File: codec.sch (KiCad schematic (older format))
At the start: 48 parts, among them J10 Audio-Jack-3, J11 MicBias, J8 Audio-Jack-3, J9 Audio-Jack-3, U2 CS4245

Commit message: [codec] Sort the input filters and add comp. values
The input filter schematic was wrong, it was using the
output's LP filter circuit (copy/paste error). All components
now have values, as per CS4245's datasheet.
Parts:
- C25, C29, C31, C33, C35, C44, C53, C54: value CP -> 10uF
- C26, C27, C28, C45, C46, C47, C48, C51, C52: value C -> 0.1uF
- C30, C32, C34, C36: value C -> 1.8nF
- C37, C39: value CP -> 3.3uF
- C41, C49, C50: value CP -> 47uF
- C42, C43: value C -> 2.2nF
- R36, R37, R38, R39, R40, R41, R42, R43: value R -> 100
- R44, R47: value R -> 470
- R45, R46: value R -> 10k
- R48: value R -> Rx
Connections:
- wire segments 87 -> 85
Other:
- moved on the sheet: C29, C30, C31, C32, C33, C34, C35, C36, R36, R37, R38, R39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

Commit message: Add power regulators with 5, 3 and 3.3V.
In addition, the connector is now as short as needed.
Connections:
- net labels added: 3.3V, 3V, 5V
- net labels removed: +3.3V, VCC
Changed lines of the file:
@@
 $EndComp
 $Comp
-L GND #PWR029
+L GND #PWR027
 U 1 1 5A0BFF3A
 P 4550 2150
-F 0 "#PWR029" H 4550 1900 50  0001 C CNN
+F 0 "#PWR027" H 4550 1900 50  0001 C CNN
 F 1 "GND" H 4550 2000 50  0000 C CNN
 F 2 "" H 4550 2150 50  0001 C CNN
@@
 $EndComp
 $Comp
-L GND #PWR030
+L GND #PWR028
 U 1 1 5A0C011B
 P 4250 5700
-F 0 "#PWR030" H 4250 5450 50  0001 C CNN
+F 0 "#PWR028" H 4250 5450 50  0001 C CNN
 F 1 "GND" H 4250 5550 50  0000 C CNN
 F 2 "" H 4250 5700 50  0001 C CNN
 F 3 "" H 4250 5700 50  0001 C CNN
 	1    4250 5700
-	1    0    0    -1
-$EndComp
-$Comp
-L +3.3V #PWR031
-U 1 1 5A0C0141
-P 4250 5400
-F 0 "#PWR031" H 4250 5250 50  0001 C CNN
-F 1 "+3.3V" H 4250 5540 50  0000 C CNN
-F 2 "" H 4250 5400 50  0001 C CNN
-F 3 "" H 4250 5400 50  0001 C CNN
-	1    4250 5400
 	1    0    0    -1
 $EndComp
@@
 $EndComp
 $Comp
-L GND #PWR032
+L GND #PWR029
 U 1 1 5A0C08B4
 P 5850 7150
-F 0 "#PWR032" H 5850 6900 50  0001 C CNN
+F 0 "#PWR029" H 5850 6900 50  0001 C CNN
 F 1 "GND" H 5850 7000 50  0000 C CNN
 F 2 "" H 5850 7150 50  0001 C CNN
@@
 AGND2
 $Comp
-L GND #PWR033
+L GND #PWR030
 U 1 1 5A0C1788
 P 7350 5250
-F 0 "#PWR033" H 7350 5000 50  0001 C CNN
+F 0 "#PWR030" H 7350 5000 50  0001 C CNN
 F 1 "GND" H 7350 5100 50  0000 C CNN
 F 2 "" H 7350 5250 50  0001 C CNN
@@
 $EndComp
 $Comp
-L GND #PWR034
+L GND #PWR031
 U 1 1 5A0C2BFF
 P 8000 4300
-F 0 "#PWR034" H 8000 4050 50  0001 C CNN
+F 0 "#PWR031" H 8000 4050 50  0001 C CNN
 F 1 "GND" H 8000 4150 50  0001 C CNN
 F 2 "" H 8000 4300 50  0001 C CNN
@@
 $EndComp
 $Comp
-L GND #PWR035
+L GND #PWR032
 U 1 1 5A0C2DDC
 P 9000 4050
-F 0 "#PWR035" H 9000 3800 50  0001 C CNN
+F 0 "#PWR032" H 9000 3800 50  0001 C CNN
 F 1 "GND" H 9000 3900 50  0000 C CNN
 F 2 "" H 9000 4050 50  0001 C CNN
@@
 $EndComp
 $Comp
-L GND #PWR036
+L GND #PWR033
 U 1 1 5A0C36C8
 P 7250 2600
-F 0 "#PWR036" H 7250 2350 50  0001 C CNN
+F 0 "#PWR033" H 7250 2350 50  0001 C CNN
 F 1 "GND" H 7250 2450 50  0001 C CNN
 F 2 "" H 7250 2600 50  0001 C CNN
@@
 $EndComp
 $Comp
-L GND #PWR037
+L GND #PWR034
 U 1 1 5A0C3B17
 P 7250 3450
-F 0 "#PWR037" H 7250 3200 50  0001 C CNN
+F 0 "#PWR034" H 7250 3200 50  0001 C CNN
 F 1 "GND" V 7250 3300 50  0001 C CNN
 F 2 "" H 7250 3450 50  0001 C CNN
@@
 $EndComp
 $Comp
-L GND #PWR038
+L GND #PWR035
 U 1 1 5A0C5076
 P 9000 2400
-F 0 "#PWR038" H 9000 2150 50  0001 C CNN
+F 0 "#PWR035" H 9000 2150 50  0001 C CNN
 F 1 "GND" H 9000 2250 50  0000 C CNN
 F 2 "" H 9000 2400 50  0001 C CNN
@@
 $EndComp
 $Comp
-L GND #PWR039
+L GND #PWR036
 U 1 1 5A0C50E0
 P 9000 3250
-F 0 "#PWR039" H 9000 3000 50  0001 C CNN
+F 0 "#PWR036" H 9000 3000 50  0001 C CNN
 F 1 "GND" H 9000 3100 50  0000 C CNN
 F 2 "" H 9000 3250 50  0001 C CNN
@@
 $EndComp
 NoConn ~ 4600 4600
-$Comp
-L VCC #PWR040
-U 1 1 5A0C5913
-P 5400 1600
-F 0 "#PWR040" H 5400 1450 50  0001 C CNN
-F 1 "VCC" H 5400 1750 50  0000 C CNN
-F 2 "" H 5400 1600 50  0001 C CNN
-F 3 "" H 5400 1600 50  0001 C CNN
-	1    5400 1600
-	1    0    0    -1
-$EndComp
 $Comp
 L C C28
@@
 $EndComp
 $Comp
-L GND #PWR041
+L GND #PWR037
 U 1 1 5A0C5A31
 P 5550 2200
-F 0 "#PWR041" H 5550 1950 50  0001 C CNN
+F 0 "#PWR037" H 5550 1950 50  0001 C CNN
 F 1 "GND" H 5550 2050 50  0000 C CNN
 F 2 "" H 5550 2200 50  0001 C CNN
@@
 $EndComp
 $Comp
-L GND #PWR042
+L GND #PWR038
 U 1 1 5A0C6D18
 P 4900 2650
-F 0 "#PWR042" H 4900 2400 50  0001 C CNN
+F 0 "#PWR038" H 4900 2400 50  0001 C CNN
 F 1 "GND" H 4900 2500 50  0000 C CNN
 F 2 "" H 4900 2650 50  0001 C CNN
@@
 	4900 2350 5200 2350
 Wire Wire Line
-	5200 2350 5200 2700
-$Comp
-L VCC #PWR043
-U 1 1 5A0C6E75
-P 5200 2350
-F 0 "#PWR043" H 5200 2200 50  0001 C CNN
-F 1 "VCC" H 5200 2500 50  0000 C CNN
-F 2 "" H 5200 2350 50  0001 C CNN
-F 3 "" H 5200 2350 50  0001 C CNN
-	1    5200 2350
-	1    0    0    -1
-$EndComp
-$Comp
-L +3.3V #PWR044
-U 1 1 5A0C6F72
-P 4550 1850
-F 0 "#PWR044" H 4550 1700 50  0001 C CNN
-F 1 "+3.3V" H 4550 1990 50  0000 C CNN
-F 2 "" H 4550 1850 50  0001 C CNN
-F 3 "" H 4550 1850 50  0001 C CNN
-	1    4550 1850
-	1    0    0    -1
-$EndComp
+	5200 2250 5200 2700
 Text HLabel 4400 4700 0    60   Output ~ 0
 PB11
@@
 	5600 2700 5600 2600
 $Comp
-L GND #PWR045
+L GND #PWR039
 U 1 1 5A0CCB20
 P 5800 2700
-F 0 "#PWR045" H 5800 2450 50  0001 C CNN
+F 0 "#PWR039" H 5800 2450 50  0001 C CNN
 F 1 "GND" H 5800 2550 50  0000 C CNN
 F 2 "" H 5800 2700 50  0001 C CNN
@@
 Wire Wire Line
 	4600 3700 4500 3700
-$Comp
-L PWR_FLAG #FLG046
-U 1 1 5A0E6115
-P 4250 5400
-F 0 "#FLG046" H 4250 5475 50  0001 C CNN
-F 1 "PWR_FLAG" H 4250 5550 50  0001 C CNN
-F 2 "" H 4250 5400 50  0001 C CNN
-F 3 "" H 4250 5400 50  0001 C CNN
-	1    4250 5400
-	-1   0    0    1
-$EndComp
 Connection ~ 8300 3450
 Connection ~ 7450 2600
@@
 Connection ~ 7450 2300
 Connection ~ 7450 2900
+Text GLabel 4250 5400 0    60   Input ~ 0
+5V
+Text GLabel 4550 1850 1    60   Input ~ 0
+3.3V
+Text GLabel 5400 1600 1    60   Input ~ 0
+3V
+Text GLabel 5200 2250 1    60   Input ~ 0
+3V
+Connection ~ 5200 2350
 $EndSCHEMATC

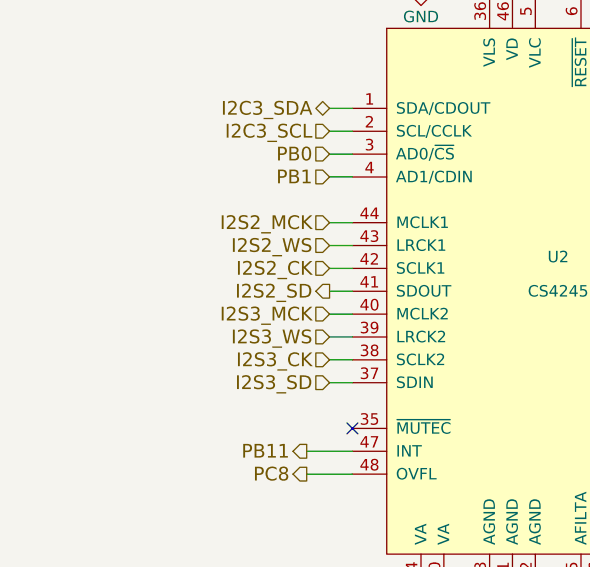
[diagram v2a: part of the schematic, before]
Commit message: Move the I2S2_SD termination resistor to driver
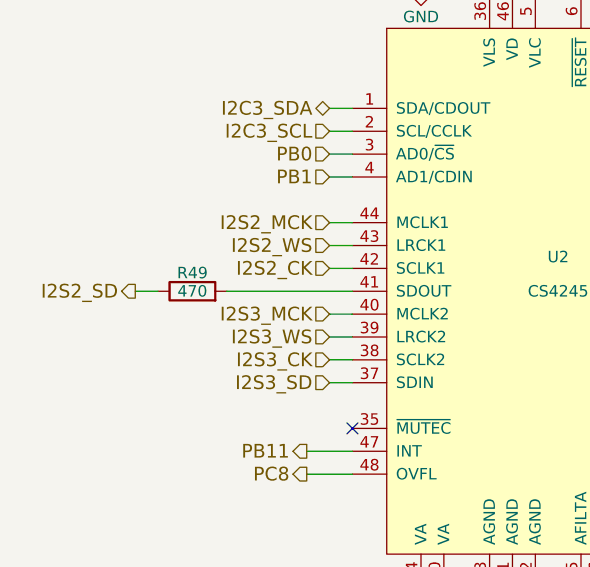
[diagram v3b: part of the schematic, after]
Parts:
- added R49: 470, symbol R
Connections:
- net I2S2_SD: now also R49.1; no longer U2.41 (SDOUT)
- new net: R49.2, U2.41 (SDOUT)
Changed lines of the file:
@@
 Text HLabel 4500 3900 0    60   Input ~ 0
 I2S2_CK
-Text HLabel 4500 4000 0    60   Output ~ 0
+Text HLabel 3650 4000 0    60   Output ~ 0
 I2S2_SD
-Wire Wire Line
-	4500 4000 4600 4000
 Wire Wire Line
 	4600 3900 4500 3900
@@
 3V
 Connection ~ 5200 2350
+$Comp
+L R R49
+U 1 1 5A18B75D
+P 3900 4000
+F 0 "R49" V 3980 4000 50  0000 C CNN
+F 1 "470" V 3900 4000 50  0000 C CNN
+F 2 "" V 3830 4000 50  0001 C CNN
+F 3 "" H 3900 4000 50  0001 C CNN
+	1    3900 4000
+	0    -1   -1   0
+$EndComp
+Wire Wire Line
+	4050 4000 4600 4000
+Wire Wire Line
+	3650 4000 3750 4000
 $EndSCHEMATC

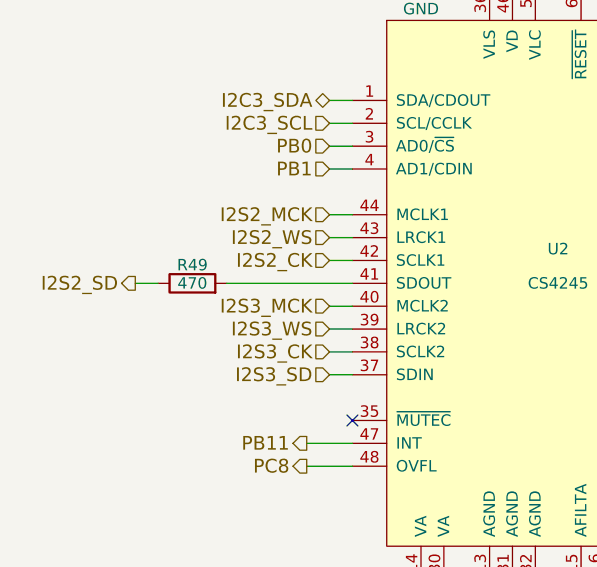
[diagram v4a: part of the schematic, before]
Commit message: Termination resistors
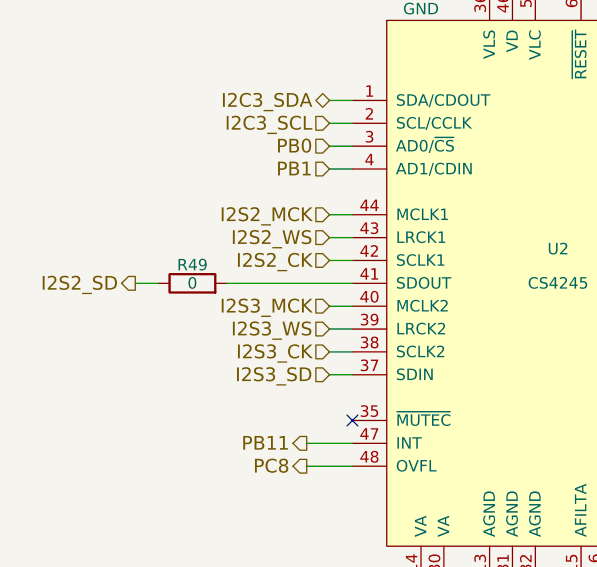
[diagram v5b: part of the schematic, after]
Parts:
- R49: value 470 -> 0
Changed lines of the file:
@@
 P 3900 4000
 F 0 "R49" V 3980 4000 50  0000 C CNN
-F 1 "470" V 3900 4000 50  0000 C CNN
+F 1 "0" V 3900 4000 50  0000 C CNN
 F 2 "" V 3830 4000 50  0001 C CNN
 F 3 "" H 3900 4000 50  0001 C CNN

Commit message: Add some of the pinouts
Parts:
- J10, J8, J9: footprint (none) -> Connectors:PJ311_3.5mm_Jack
- J11: footprint (none) -> Pin_Headers:Pin_Header_Straight_1x02
- U2: footprint (none) -> Housings_QFP:LQFP-48_7x7mm_Pitch0.5mm
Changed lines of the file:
@@
 F 0 "U2" H 5500 4150 50  0000 C CNN
 F 1 "CS4245" H 5500 4000 50  0000 C CNN
-F 2 "" H 5500 4350 50  0001 C CNN
+F 2 "Housings_QFP:LQFP-48_7x7mm_Pitch0.5mm" H 5500 4350 50  0001 C CNN
 F 3 "" H 5500 4350 50  0001 C CNN
 	1    5500 4000
@@
 F 0 "J11" H 7650 4900 50  0000 C CNN
 F 1 "MicBias" H 7650 4600 50  0000 C CNN
-F 2 "" H 7650 4800 50  0001 C CNN
+F 2 "Pin_Headers:Pin_Header_Straight_1x02" H 7650 4800 50  0001 C CNN
 F 3 "" H 7650 4800 50  0001 C CNN
 	1    7650 4800
@@
 F 0 "J9" H 8750 3525 50  0000 C CNN
 F 1 "Audio-Jack-3" H 8900 3280 50  0000 C CNN
-F 2 "" H 9050 3450 50  0001 C CNN
+F 2 "Connectors:PJ311_3.5mm_Jack" H 9050 3450 50  0001 C CNN
 F 3 "" H 9050 3450 50  0001 C CNN
 	1    8800 3350
@@
 F 0 "J10" H 8750 4325 50  0000 C CNN
 F 1 "Audio-Jack-3" H 8900 4080 50  0000 C CNN
-F 2 "" H 9050 4250 50  0001 C CNN
+F 2 "Connectors:PJ311_3.5mm_Jack" H 9050 4250 50  0001 C CNN
 F 3 "" H 9050 4250 50  0001 C CNN
 	1    8800 4150
@@
 F 0 "J8" H 8750 2675 50  0000 C CNN
 F 1 "Audio-Jack-3" H 8900 2430 50  0000 C CNN
-F 2 "" H 9050 2600 50  0001 C CNN
+F 2 "Connectors:PJ311_3.5mm_Jack" H 9050 2600 50  0001 C CNN
 F 3 "" H 9050 2600 50  0001 C CNN
 	1    8800 2500

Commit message: Add remaining footprints
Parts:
- C25, C29, C31, C33, C35, C37, C39, C44, C53: footprint (none) -> Capacitors_SMD:c_elec_4x4.5
- C26, C27, C28, C30, C32, C34, C36, C38, C40, C42, C43, C45, C46, C47, C48, C51, C52: footprint (none) -> Capacitors_SMD:C_0805_HandSoldering
- C41, C49, C50: footprint (none) -> Capacitors_SMD:c_elec_6.3x7.7
- C54: footprint (none) -> Capacitors_SMD:C_2225_HandSoldering
- R36, R37, R38, R39, R40, R41, R42, R43, R44, R45, R46, R47, R48, R49: footprint (none) -> Resistors_SMD:R_0805_HandSoldering
